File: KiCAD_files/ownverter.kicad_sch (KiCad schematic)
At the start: 13 parts, among them J101 Harting-15 and Wago 6

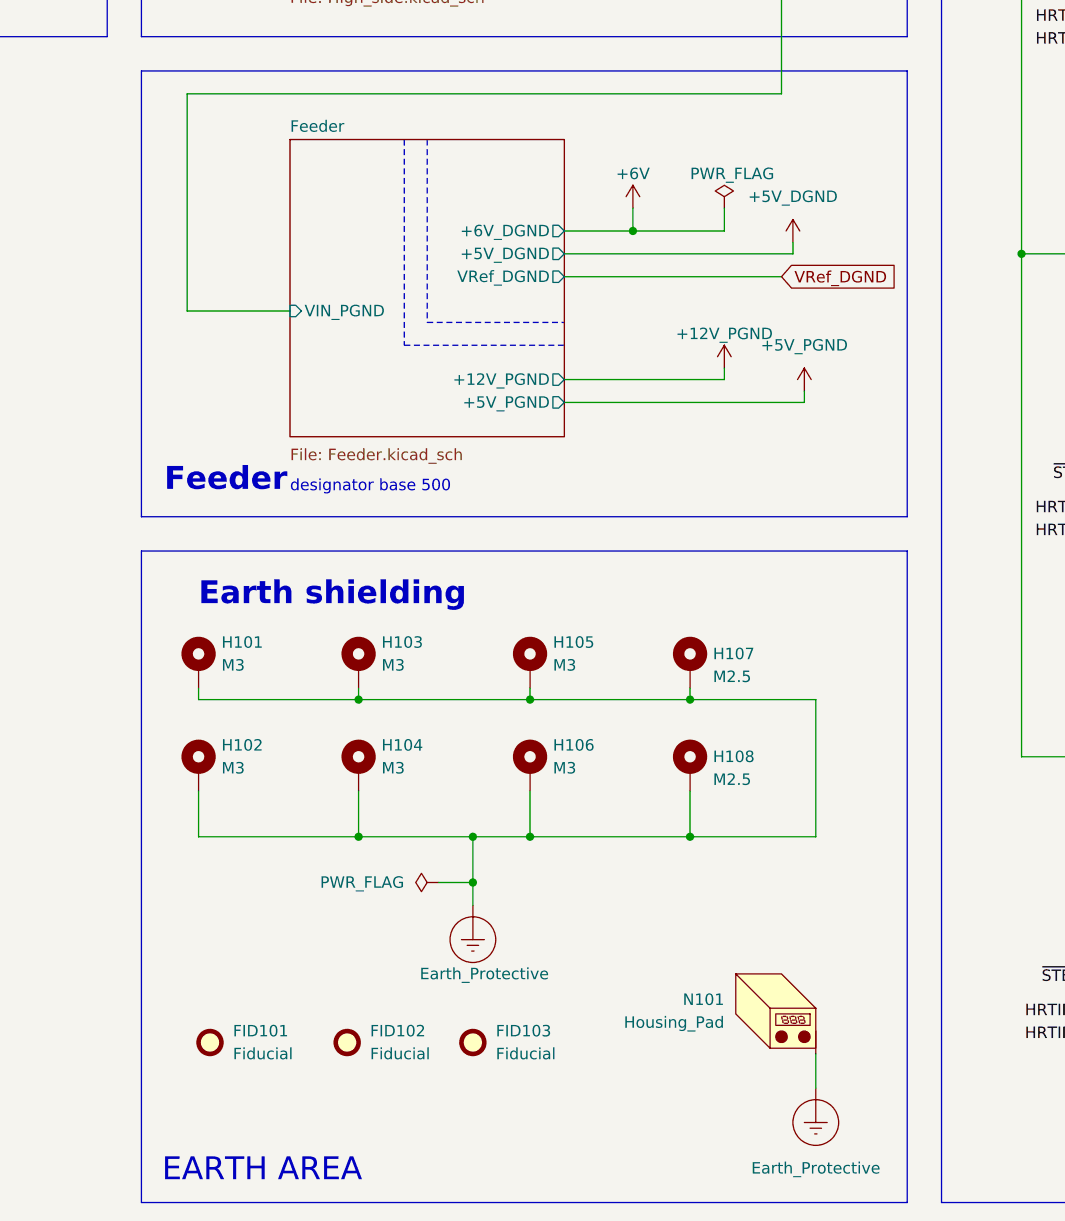
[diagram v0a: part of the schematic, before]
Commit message: OWNVERTER V1.0.0 - bumped to kiCAD 9
Signed-off-by: Jean Alinei <jean.alinei@owntech.org>
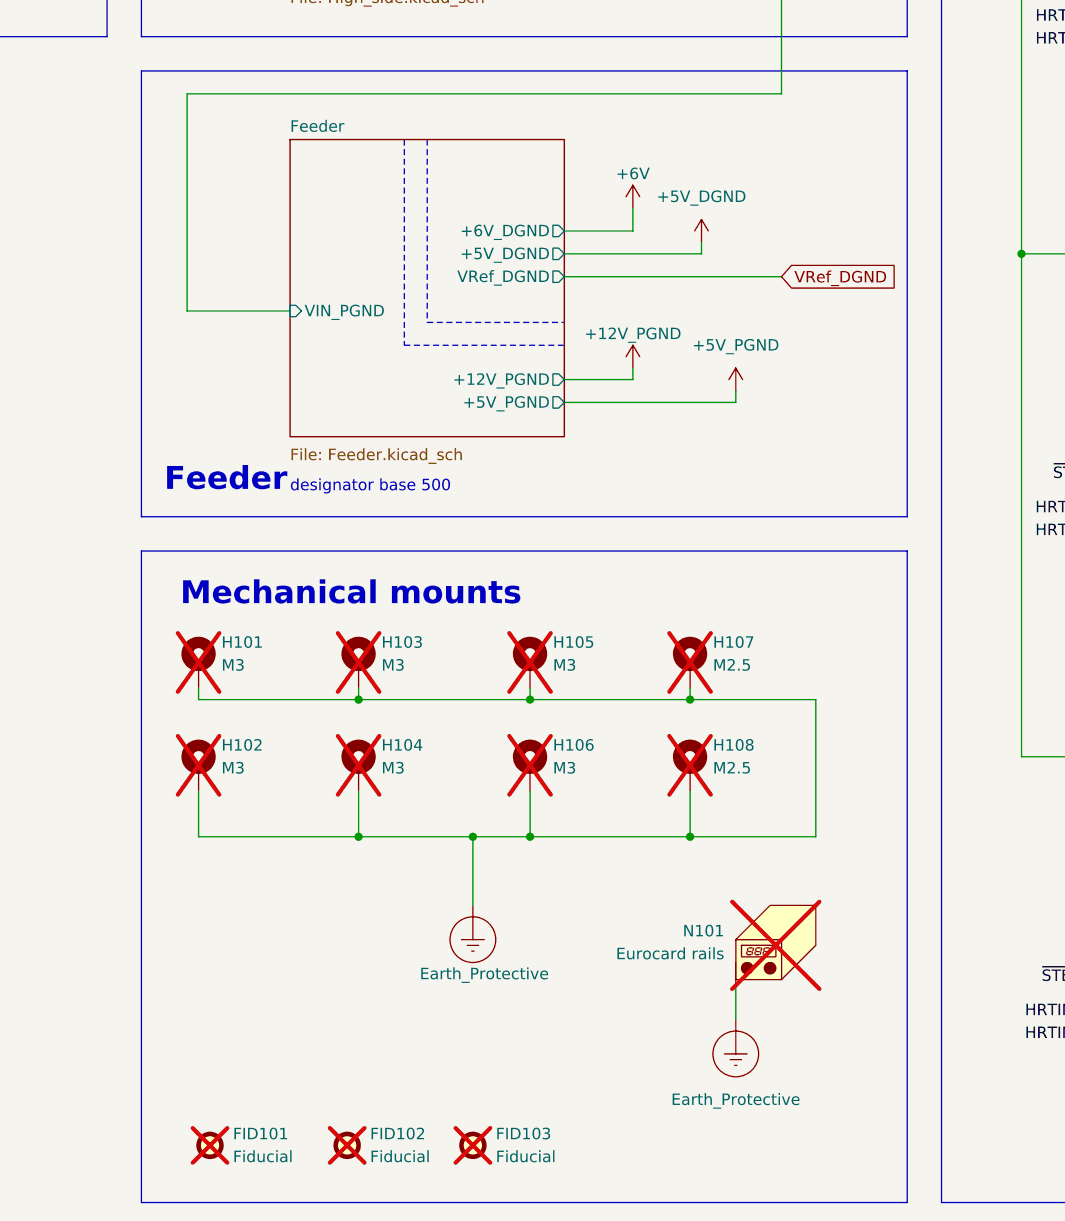
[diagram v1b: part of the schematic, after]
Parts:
- FID101, FID102, FID103: now not fitted; now left out of the parts list
- H101, H102, H103, H104, H105, H106, H107, H108: now not fitted
- N101: value Housing_Pad -> Eurocard rails; now not fitted
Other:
- note added: "Mechanical mounts"
- note removed: "EARTH AREA"
- note removed: "Earth shielding"
- title: OWNVERTER V1.1 -> OWNVERTER V1.0

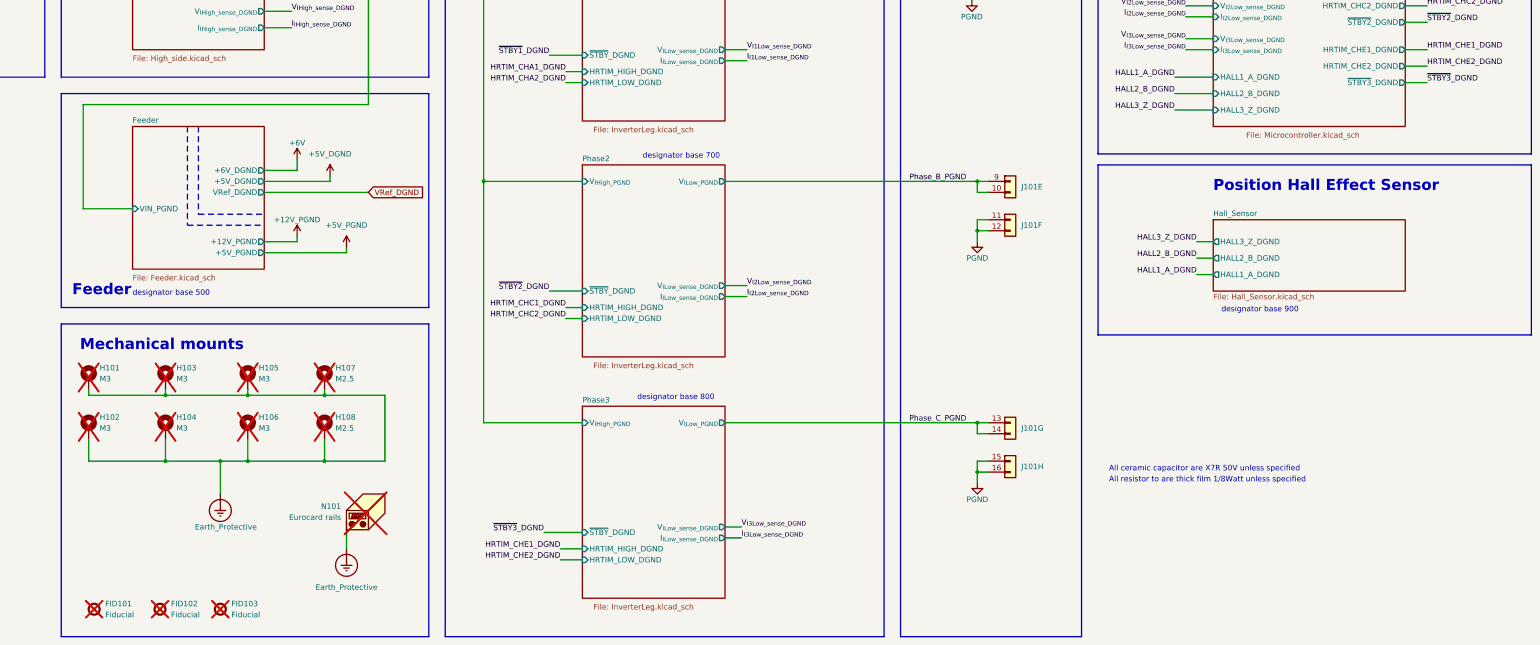
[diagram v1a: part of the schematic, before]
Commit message: Placement mostly done, ready for routing.
Signed-off-by: Jean Alinei <jean.alinei@owntech.org>
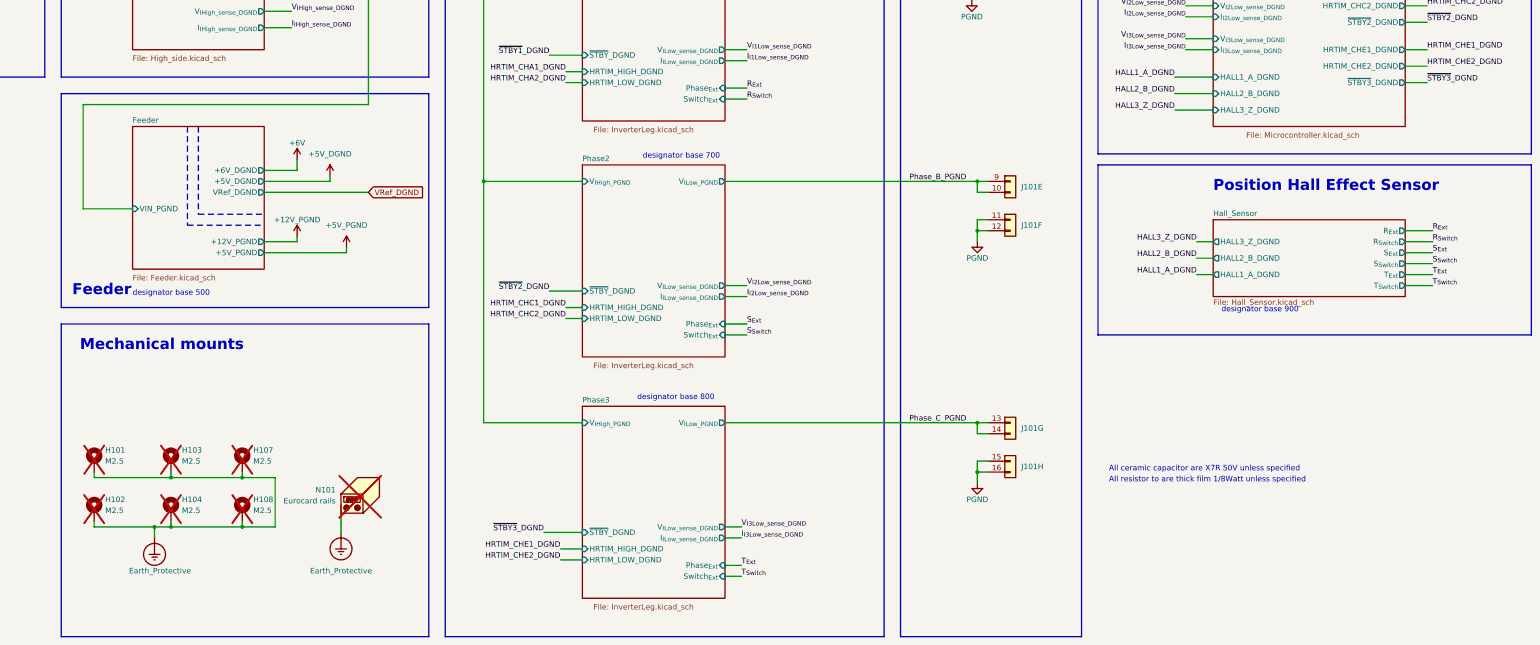
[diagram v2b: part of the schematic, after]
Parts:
- removed FID101, FID102, FID103: Fiducial, Fiducial:Fiducial_0.75mm_Mask1.5mm, symbol Mechanical:Fiducial
- removed H105, H106: M3, MountingHole:MountingHole_3.2mm_M3_DIN965_Pad_TopOnly, symbol Mechanical:MountingHole_Pad
- H101, H102, H103, H104: value M3 -> M2.5; footprint MountingHole:MountingHole_3.2mm_M3_DIN965_Pad_TopOnly -> MountingHole:MountingHole_2.7mm_M2.5_DIN965_Pad_TopOnly; DNP x -> (none)
- H107, H108, N101: DNP x -> (none)
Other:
- sheet Hall_Sensor ports: added R_{Ext}, R_{Switch}, S_{Ext}, S_{Switch}, T_{Ext}, T_{Switch}; removed none
- sheet Phase1 ports: added Phase_{Ext}, Switch_{Ext}; removed none
- sheet Phase2 ports: added Phase_{Ext}, Switch_{Ext}; removed none
- sheet Phase3 ports: added Phase_{Ext}, Switch_{Ext}; removed none
- moved on the sheet: H101, H102, H103, H104, H107, H108, N101

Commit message: OWNVERTER V1.1.0 as built
Signed-off-by: Jean Alinei <jean.alinei@owntech.org>
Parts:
- removed unit 5 of J101
- removed unit 6 of J101
- removed unit 4 of J101
- removed unit 1 of J101
- removed unit 7 of J101
- removed unit 8 of J101
- removed unit 3 of J101
- added unit 3 of J101
- added unit 1 of J101
- added J103: Harting-15 and Wago 6, Footprints:WAGO-2604-1106, symbol Symbols:Harting 15 contacts WAGO 6
- added J104: 2604-1102, Footprints:WAGO-2604-1102, symbol Symbols:WAGO 2 contacts
- added J105: 2604-1102, Footprints:WAGO-2604-1102_1, symbol Symbols:WAGO 2 contacts
- J101: footprint Footprints:Harting - 15contacts and Wago -> Footprints:Harting - 15contacts and Wago_1_1; symbol Symbols:Harting 15 contacts and WAGO -> Symbols:Harting 15 contacts and WAGO_1; now not fitted; now left out of the parts list
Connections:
- net High_side/V_{IHighIN_PGND}: now also J103.1 (Pin_1), J103.2 (Pin_2)
- net PGND: now also J101.11 (Pin_1), J101.12 (Pin_2), J101.15 (Pin_1), J101.16 (Pin_2), J101.7 (Pin_1), J101.8 (Pin_2), J103.3 (Pin_3), J103.4 (Pin_4); no longer J101.3 (Pin_1), J101.4 (Pin_2)
- net Phase_A_PGND: now also J103.5 (Pin_1), J103.6 (Pin_2)
- net Phase_B_PGND: now also J104.10 (Pin_2), J104.9 (Pin_1)
- net Phase_C_PGND: now also J105.13 (Pin_1), J105.14 (Pin_2)
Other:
- note added: "Connexions for optional backplane connector"
- title: OWNVERTER V1.0 -> OWNVERTER V1.1
- moved on the sheet: H101, H102, H103, H104, H107, H108, N101

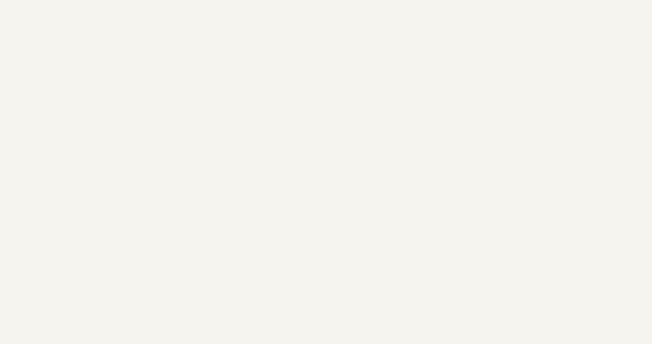
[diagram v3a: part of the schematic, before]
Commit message: Bumping to v1.1.1 - Bug fixes and silkscreen enhancement.
Signed-off-by: Jean Alinei <jean.alinei@owntech.org>
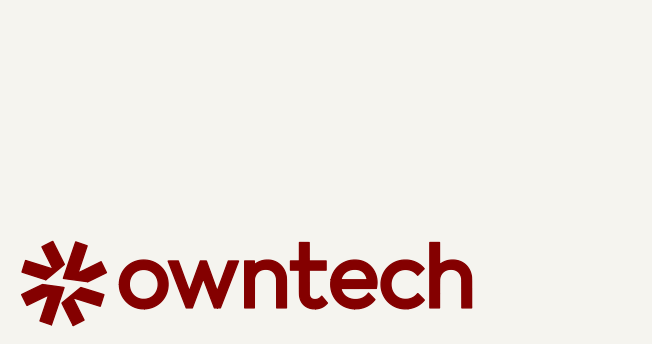
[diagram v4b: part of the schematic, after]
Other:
- title: OWNVERTER V1.1 -> OWNVERTER V1.1.1
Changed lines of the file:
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@@
 	(paper "A3")
 	(title_block
-		(title "OWNVERTER V1.1")
-		(date "2025-04-24")
-		(comment 1 "ALINEI")
+		(title "OWNVERTER V1.1.1")
+		(date "2025-10-13")
+		(comment 1 "JAL")
+		(comment 2 "LFL")
+		(comment 3 "LFL")
 		(comment 4 "GFE")
 	)
@@
 					(unit 1)
 				)
+			)
+		)
+	)
+	(symbol
+		(lib_id "Symbols:LOGO")
+		(at 41.91 276.86 0)
+		(unit 1)
+		(exclude_from_sim no)
+		(in_bom yes)
+		(on_board yes)
+		(dnp no)
+		(fields_autoplaced yes)
+		(property "Reference" "#G201"
+			(at 41.91 272.8146 0)
+			(effects
+				(font
+					(size 1.27 1.27)
+				)
+				(hide yes)
+			)
+		)
+		(property "Value" "LOGO"
+			(at 41.91 280.9054 0)
+			(effects
+				(font
+					(size 1.27 1.27)
+				)
+				(hide yes)
+			)
+		)
+		(property "Footprint" ""
+			(at 41.91 276.86 0)
+			(effects
+				(font
+					(size 1.27 1.27)
+				)
+				(hide yes)
+			)
+		)
+		(property "Datasheet" ""
+			(at 41.91 276.86 0)
+			(effects
+				(font
+					(size 1.27 1.27)
+				)
+				(hide yes)
+			)
+		)
+		(property "Description" ""
+			(at 41.91 276.86 0)
+			(effects
+				(font
+					(size 1.27 1.27)
+				)
+				(hide yes)
+			)
+		)
+		(instances
+			(project ""
+				(path "/8d0c1d66-35ef-4a53-a28f-436a11b54f42"
+					(reference "#G201")
+					(unit 1)
+				)
